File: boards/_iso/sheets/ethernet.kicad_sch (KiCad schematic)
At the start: 11 parts, among them J1 RJHSE5380, T1 HX5008NLT

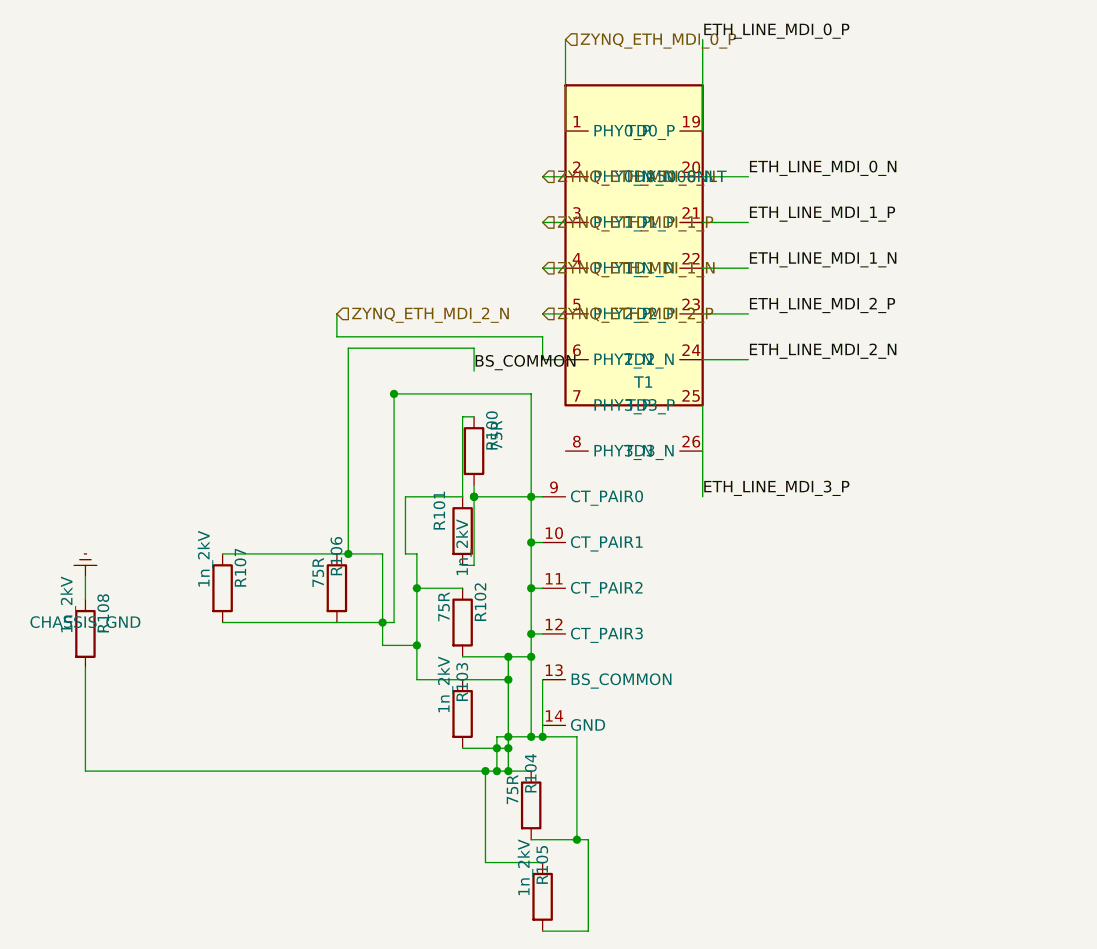
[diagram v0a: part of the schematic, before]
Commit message: Regenerate carrier (overlap=0 all 27, ERC 134->22) + STAGE_E_STATUS UPDATE 4
Co-Authored-By: Claude Opus 4.8 <noreply@anthropic.com>
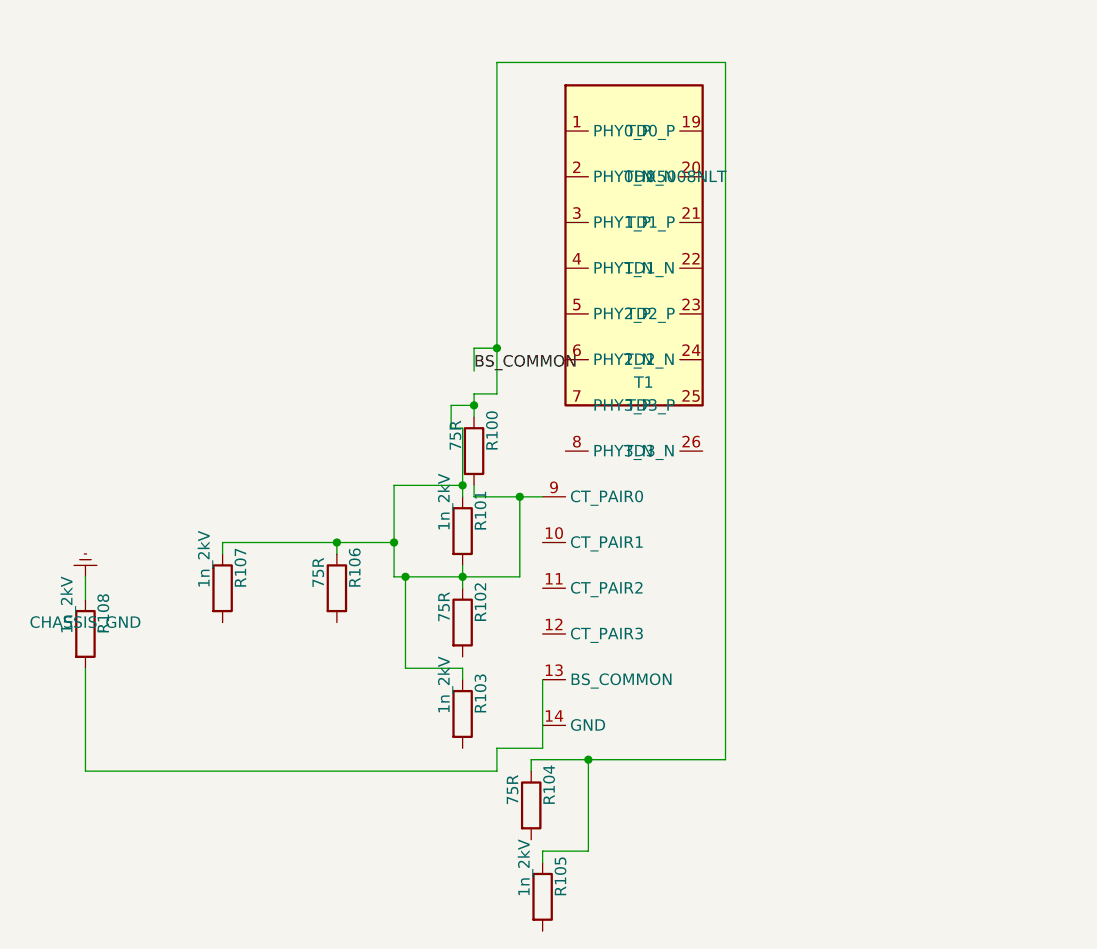
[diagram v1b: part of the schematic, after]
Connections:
- net BS_COMMON: no longer R102.2, R103.2, R104.2, R105.2, R106.2, R107.2, R108.2, T1.10 (CT_PAIR1), T1.11 (CT_PAIR2), T1.12 (CT_PAIR3), T1.13 (BS_COMMON), T1.14 (GND)
- net ETH_LINE_MDI_0_N: no longer T1.20 (TD0_N)
- net ETH_LINE_MDI_0_P: no longer T1.19 (TD0_P)
- net ETH_LINE_MDI_1_N: no longer T1.22 (TD1_N)
- net ETH_LINE_MDI_1_P: no longer T1.21 (TD1_P)
- net ETH_LINE_MDI_2_N: no longer T1.24 (TD2_N)
- net ETH_LINE_MDI_2_P: no longer T1.23 (TD2_P)
- net ETH_LINE_MDI_3_P: no longer T1.25 (TD3_P), T1.26 (TD3_N)
- net ZYNQ_ETH_MDI_0_N: no longer names the net of T1.2 (PHY0_N)
- net ZYNQ_ETH_MDI_0_P: no longer names the net of T1.1 (PHY0_P)
- net ZYNQ_ETH_MDI_1_N: no longer names the net of T1.4 (PHY1_N)
- net ZYNQ_ETH_MDI_1_P: no longer names the net of T1.3 (PHY1_P)
- net ZYNQ_ETH_MDI_2_N: no longer names the net of T1.6 (PHY2_N)
- net ZYNQ_ETH_MDI_2_P: no longer names the net of T1.5 (PHY2_P)
- new net: R108.2, T1.13 (BS_COMMON), T1.14 (GND)
